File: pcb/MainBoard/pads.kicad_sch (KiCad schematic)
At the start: 35 parts

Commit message: pcb: main board - contd
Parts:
- added JP? (x2): SolderJumper_2_Open, Jumper:SolderJumper-2_P1.3mm_Open_RoundedPad1.0x1.5mm, symbol Jumper:SolderJumper_2_Open
- added JP?: SolderJumper_3_Open, Jumper:SolderJumper-3_P1.3mm_Open_RoundedPad1.0x1.5mm, symbol Jumper:SolderJumper_3_Open
- added Q?: HL2304, PCM_Package_TO_SOT_SMD_AKL:SOT-23, symbol Device:Q_NMOS_GSD
- added R? (x6): 10k, Resistor_SMD:R_0402_1005Metric, symbol Device:R
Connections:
- net +3V3: now also JP?.2 (B), Q?.1 (G), R?.1, R?.1; no longer D?.1 (A1), J?.1 (Pin_1)
- net +5V: now also JP?.2 (B), R?.1
- net COL_RCLK: no longer J?.1 (Pin_1)
- net COL_SER: now also JP?.1 (A), Q?.2 (S), R?.2; no longer J?.1 (Pin_1)
- net COL_SRCLK: no longer J?.1 (Pin_1)
- net COL_~{OE}: now also R?.2; no longer J?.1 (Pin_1)
- net COL_~{SRCLR}: now also R?.1; no longer J?.1 (Pin_1)
- net GND: now also R?.2, R?.2
- net ROW_~{OE}: now also R?.2
- net ROW_~{SRCLR}: now also R?.1
- new net COL_RCLK_OUT: J?.1 (Pin_1)
- new net COL_SER_5V: JP?.3 (B), Q?.3 (D), R?.2
- new net COL_SER_OUT: J?.1 (Pin_1), JP?.2 (C)
- new net COL_SRCLK_OUT: J?.1 (Pin_1)
- new net COL_VCC: D?.1 (A1), J?.1 (Pin_1), JP?.1 (A), JP?.1 (A), R?.1
- new net COL_~{OE}_OUT: J?.1 (Pin_1)
- new net COL_~{SRCLR}_OUT: J?.1 (Pin_1)
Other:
- note added: "clear and disable output by default"
- note added: "rows don't need vled"
- moved on the sheet: D?, J?, R?

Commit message: pcb progress
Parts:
- D501, D502, D503, D504, D505, D506, D507, D508, D509, D510, D511, D512, D513, D514: renamed from D?; footprint can:DFN1006_TVS -> led-matrix:DFN1006_TVS
- gave numbers to parts that had none: 31

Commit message: dump pcb
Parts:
- removed JP501, JP502: SolderJumper_2_Open, Jumper:SolderJumper-2_P1.3mm_Open_RoundedPad1.0x1.5mm, symbol Jumper:SolderJumper_2_Open
- added C501, C504, C505: 22u, Capacitor_SMD:C_0805_2012Metric, symbol Device:C
- added C502: 470u, Capacitor_SMD:CP_Elec_8x10.5, symbol Device:C_Polarized
- added C503: 100u, Capacitor_Tantalum_SMD:CP_EIA-3528-15_AVX-H, symbol Device:C_Polarized
- added H501, H502, H503, H504: JLCToolingHole, led-matrix:jlcpcb-tooling-hole, symbol Mechanical:MountingHole
- added JP501, JP502, JP504, JP505, JP506, JP507, JP508, JP509: SolderJumper_3_Open, led-matrix:SolderJumper-3_Open_RoundedPad_Smol, symbol Jumper:SolderJumper_3_Open
- added Q502, Q503, Q504, Q505, Q506, Q507: HL2304, Package_TO_SOT_SMD:SOT-23, symbol Device:Q_NMOS_GSD
- added R508, R510, R512, R513, R515: 4k7, Resistor_SMD:R_0402_1005Metric, symbol Device:R
- added R509, R511, R514: 10k, Resistor_SMD:R_0402_1005Metric, symbol Device:R
- JP503: footprint Jumper:SolderJumper-3_P1.3mm_Open_RoundedPad1.0x1.5mm -> led-matrix:SolderJumper-3_Open_RoundedPad_Smol
- Q501: footprint PCM_Package_TO_SOT_SMD_AKL:SOT-23 -> Package_TO_SOT_SMD:SOT-23
- R501, R507: value 10k -> 4k7; LCSC C25744 -> C25900
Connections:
- net +3V3: now also C501.1, C505.1, JP501.1 (A), Q507.1 (G), R514.1
- net +5V: now also R501.1, C502.1, C503.1, JP501.3 (B), JP504.1 (A), R508.1, R510.1, R512.1, R513.1, R515.1
- net COL_RCLK: now also JP502.1 (A), Q502.1 (G), R509.1; no longer D507.1 (A1)
- net COL_RCLK_OUT: now also D507.1 (A1), JP502.2 (C)
- net COL_SER: now also JP507.1 (A), Q505.1 (G); no longer D505.1 (A1), JP503.1 (A)
- net COL_SER_5V: now also Q505.3 (D); no longer Q501.3 (D)
- net COL_SER_OUT: now also D505.1 (A1), JP507.2 (C); no longer JP503.2 (C)
- net COL_SRCLK: now also JP506.1 (A), Q504.1 (G), R511.1; no longer D508.1 (A1)
- net COL_SRCLK_OUT: now also D508.1 (A1), JP506.2 (C)
- net COL_VCC: now also C504.1, JP501.2 (C); no longer R501.1
- net COL_~{OE}: now also R504.1, JP505.1 (A), Q503.1 (G); no longer D506.1 (A1), R501.2
- net COL_~{OE}_OUT: now also D506.1 (A1), JP505.2 (C)
- net COL_~{SRCLR}: now also JP509.1 (A), Q506.1 (G), Q507.2 (S), R514.2; no longer D509.1 (A1), R504.1
- net COL_~{SRCLR}_OUT: now also D509.1 (A1), JP509.2 (C)
- net GND: now also C501.2, C502.2, C503.2, C504.2, C505.2, Q502.2 (S), Q503.2 (S), Q504.2 (S), Q505.2 (S), Q506.2 (S), R509.2, R511.2
- net ROW_VLED: now also JP504.2 (C); no longer R503.1
- new net: JP503.2 (C), JP507.3 (B)
- new net: JP504.3 (B), R503.1
- new net: JP508.2 (C), JP509.3 (B)
- new net COL_RCLK_5V: JP502.3 (B), Q502.3 (D), R508.2
- new net COL_SER_5V_BIDI: JP503.1 (A), Q501.3 (D), R512.2
- new net COL_SRCLK_5V: JP506.3 (B), Q504.3 (D), R510.2
- new net COL_~{OE}_5V: JP505.3 (B), Q503.3 (D), R501.2
- new net COL_~{SRCLR}_5V: JP508.3 (B), Q506.3 (D), R513.2
- new net COL_~{SRCLR}_5V_BIDI: JP508.1 (A), Q507.3 (D), R515.2
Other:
- note added: "rows don't need vled… I think"
- note removed: "rows don't need vled"
- moved on the sheet: J501, J502, J503, J504, J505, J506, J507, J508, J509, J510, J511, J512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

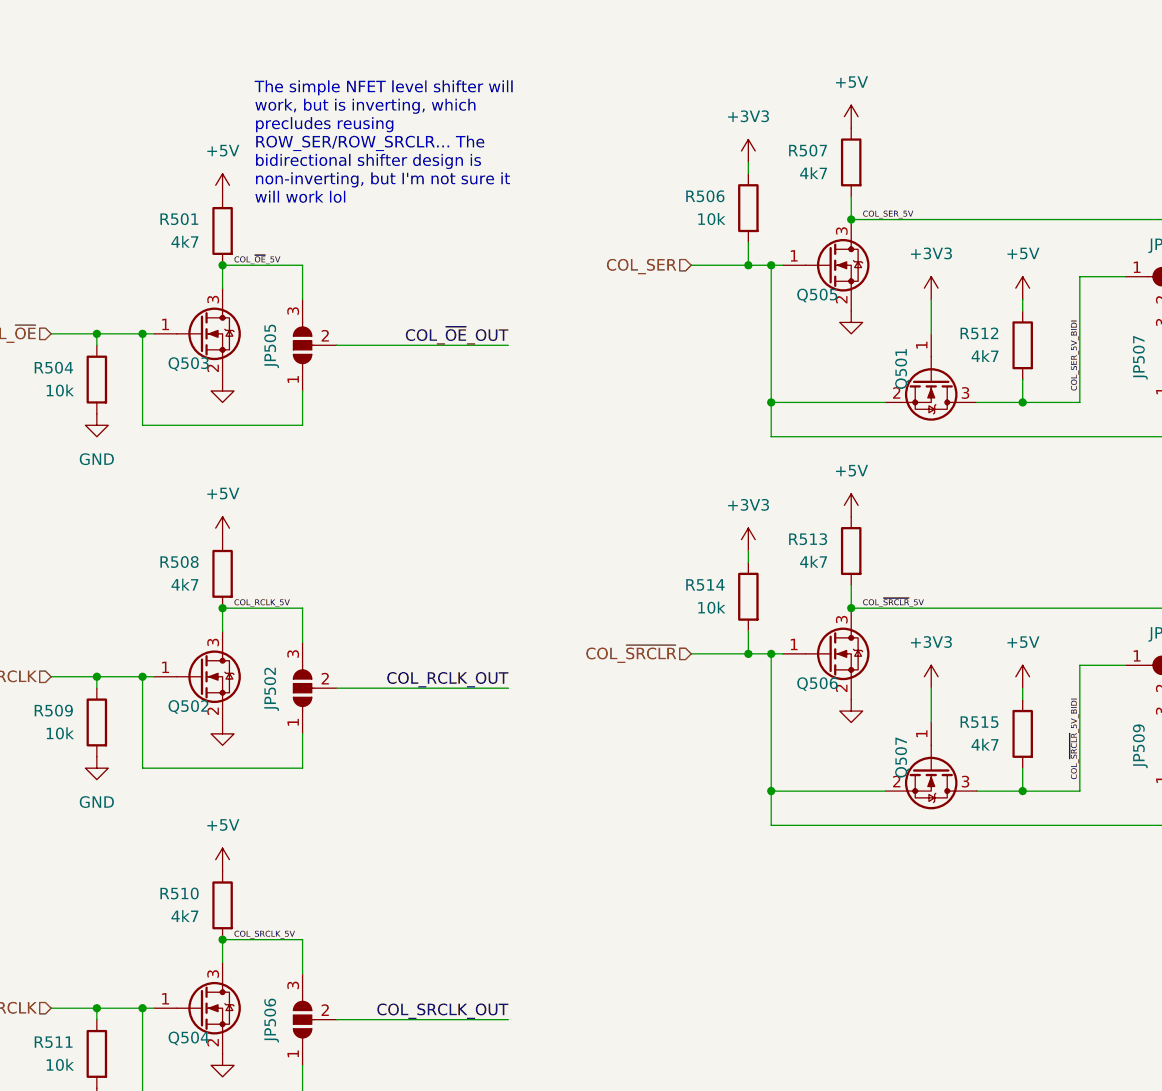
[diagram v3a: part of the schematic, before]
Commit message: MainBoard: fixes, simplify, BOM optimize, DRC fixes, ERC fixes
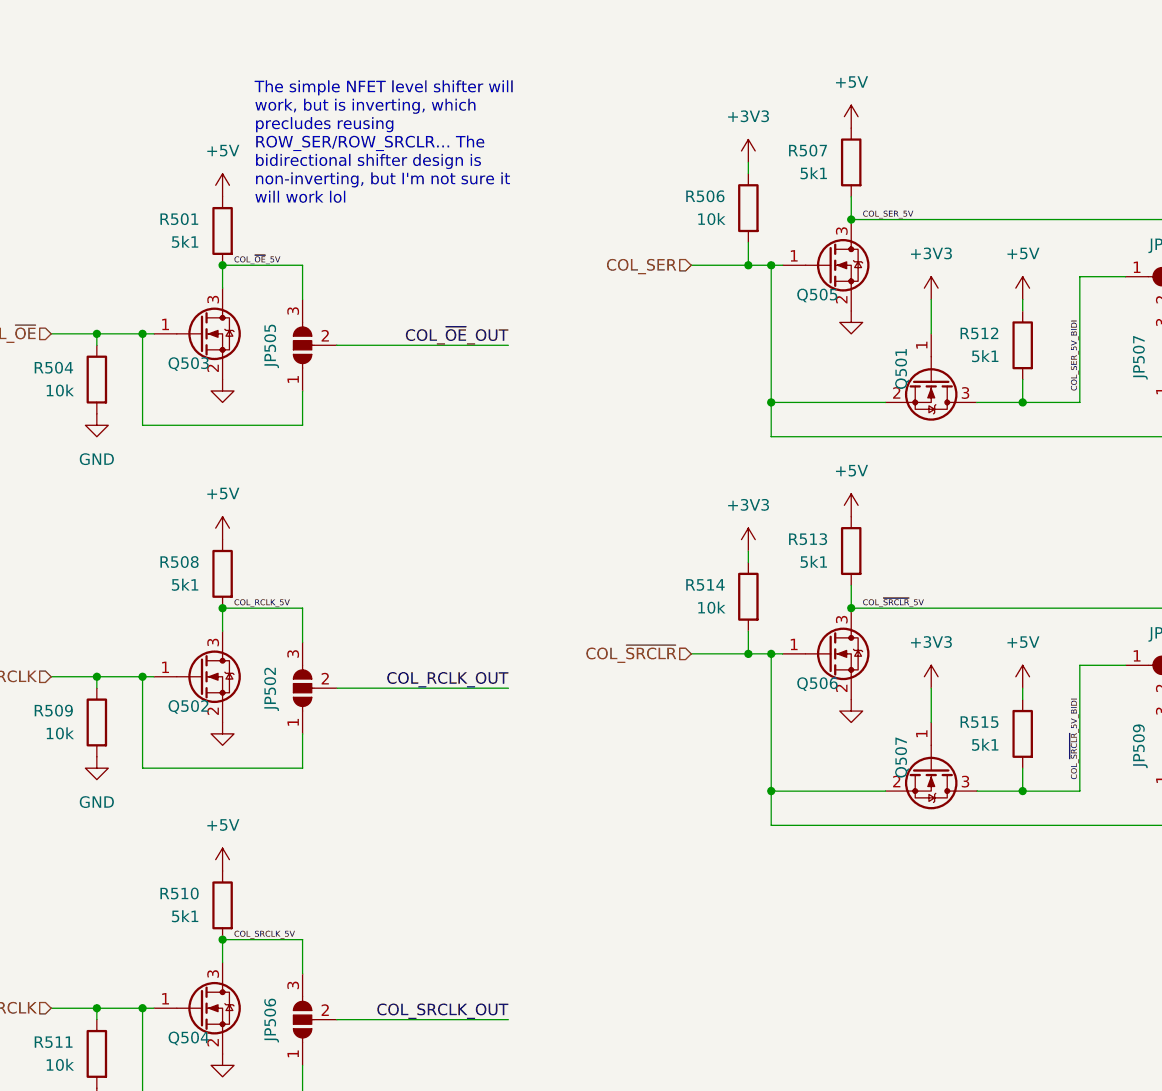
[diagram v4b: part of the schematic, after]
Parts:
- J501, J502, J503, J504, J505, J506, J507, J508, J509, J510, J511, J512, J513, J514, J515, J516, J517, J518, J519, J520, JP501, JP502, JP503, JP504, JP505, JP506, JP507, JP508, JP509: now left out of the parts list
- R501, R507, R508, R510, R512, R513, R515: value 4k7 -> 5k1; LCSC C25900 -> C25905
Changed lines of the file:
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@@
 		(unit 1)
 		(exclude_from_sim no)
-		(in_bom yes)
+		(in_bom no)
 		(on_board yes)
 		(dnp no)
@@
 			)
 		)
-		(property "Value" "4k7"
+		(property "Value" "5k1"
 			(at 91.44 96.5199 0)
 			(effects
@@
 			)
 		)
-		(property "LCSC" "C25900"
+		(property "LCSC" "C25905"
 			(at 93.98 95.25 0)
 			(effects
@@
 		(unit 1)
 		(exclude_from_sim no)
-		(in_bom yes)
+		(in_bom no)
 		(on_board yes)
 		(dnp no)
@@
 		(unit 1)
 		(exclude_from_sim no)
-		(in_bom yes)
+		(in_bom no)
 		(on_board yes)
 		(dnp no)
@@
 		(unit 1)
 		(exclude_from_sim no)
-		(in_bom yes)
+		(in_bom no)
 		(on_board yes)
 		(dnp no)
@@
 		(unit 1)
 		(exclude_from_sim no)
-		(in_bom yes)
+		(in_bom no)
 		(on_board yes)
 		(dnp no)
@@
 			)
 		)
-		(property "Value" "4k7"
+		(property "Value" "5k1"
 			(at 161.29 88.8999 0)
 			(effects
@@
 			)
 		)
-		(property "LCSC" "C25900"
+		(property "LCSC" "C25905"
 			(at 163.83 87.63 0)
 			(effects
@@
 		(unit 1)
 		(exclude_from_sim no)
-		(in_bom yes)
+		(in_bom no)
 		(on_board yes)
 		(dnp no)
@@
 		(unit 1)
 		(exclude_from_sim no)
-		(in_bom yes)
+		(in_bom no)
 		(on_board yes)
 		(dnp no)
@@
 		(unit 1)
 		(exclude_from_sim no)
-		(in_bom yes)
+		(in_bom no)
 		(on_board yes)
 		(dnp no)
@@
 		(unit 1)
 		(exclude_from_sim no)
-		(in_bom yes)
+		(in_bom no)
 		(on_board yes)
 		(dnp no)
@@
 		(unit 1)
 		(exclude_from_sim no)
-		(in_bom yes)
+		(in_bom no)
 		(on_board yes)
 		(dnp no)
@@
 			)
 		)
-		(property "Value" "4k7"
+		(property "Value" "5k1"
 			(at 161.29 132.0799 0)
 			(effects
@@
 			)
 		)
-		(property "LCSC" "C25900"
+		(property "LCSC" "C25905"
 			(at 163.83 130.81 0)
 			(effects
@@
 		(unit 1)
 		(exclude_from_sim no)
-		(in_bom yes)
+		(in_bom no)
 		(on_board yes)
 		(dnp no)
@@
 		(unit 1)
 		(exclude_from_sim no)
-		(in_bom yes)
+		(in_bom no)
 		(on_board yes)
 		(dnp no)
@@
 		(unit 1)
 		(exclude_from_sim no)
-		(in_bom yes)
+		(in_bom no)
 		(on_board yes)
 		(dnp no)
@@
 		(unit 1)
 		(exclude_from_sim no)
-		(in_bom yes)
+		(in_bom no)
 		(on_board yes)
 		(dnp no)
@@
 		(unit 1)
 		(exclude_from_sim no)
-		(in_bom yes)
+		(in_bom no)
 		(on_board yes)
 		(dnp no)
@@
 		(unit 1)
 		(exclude_from_sim no)
-		(in_bom yes)
+		(in_bom no)
 		(on_board yes)
 		(dnp no)
@@
 		(unit 1)
 		(exclude_from_sim no)
-		(in_bom yes)
+		(in_bom no)
 		(on_board yes)
 		(dnp no)
@@
 			)
 		)
-		(property "Value" "4k7"
+		(property "Value" "5k1"
 			(at 180.34 109.2199 0)
 			(effects
@@
 			)
 		)
-		(property "LCSC" "C25900"
+		(property "LCSC" "C25905"
 			(at 182.88 107.95 0)
 			(effects
@@
 		(unit 1)
 		(exclude_from_sim no)
-		(in_bom yes)
+		(in_bom no)
 		(on_board yes)
 		(dnp no)
@@
 			)
 		)
-		(property "Value" "4k7"
+		(property "Value" "5k1"
 			(at 180.34 152.3999 0)
 			(effects
@@
 			)
 		)
-		(property "LCSC" "C25900"
+		(property "LCSC" "C25905"
 			(at 182.88 151.13 0)
 			(effects
@@
 		(unit 1)
 		(exclude_from_sim no)
-		(in_bom yes)
+		(in_bom no)
 		(on_board yes)
 		(dnp no)
@@
 			)
 		)
-		(property "Value" "4k7"
+		(property "Value" "5k1"
 			(at 91.44 171.4499 0)
 			(effects
@@
 			)
 		)
-		(property "LCSC" "C25900"
+		(property "LCSC" "C25905"
 			(at 93.98 170.18 0)
 			(effects
@@
 		(unit 1)
 		(exclude_from_sim no)
-		(in_bom yes)
+		(in_bom no)
 		(on_board yes)
 		(dnp no)
@@
 		(unit 1)
 		(exclude_from_sim no)
-		(in_bom yes)
+		(in_bom no)
 		(on_board yes)
 		(dnp no)
@@
 			)
 		)
-		(property "Value" "4k7"
+		(property "Value" "5k1"
 			(at 91.44 134.6199 0)
 			(effects
@@
 			)
 		)
-		(property "LCSC" "C25900"
+		(property "LCSC" "C25905"
 			(at 93.98 133.35 0)
 			(effects
@@
 		(unit 1)
 		(exclude_from_sim no)
-		(in_bom yes)
+		(in_bom no)
 		(on_board yes)
 		(dnp no)
@@
 		(unit 1)
 		(exclude_from_sim no)
-		(in_bom yes)
+		(in_bom no)
 		(on_board yes)
 		(dnp no)
@@
 		(unit 1)
 		(exclude_from_sim no)
-		(in_bom yes)
+		(in_bom no)
 		(on_board yes)
 		(dnp no)
@@
 		(unit 1)
 		(exclude_from_sim no)
-		(in_bom yes)
+		(in_bom no)
 		(on_board yes)
 		(dnp no)
@@
 		(unit 1)
 		(exclude_from_sim no)
-		(in_bom yes)
+		(in_bom no)
 		(on_board yes)
 		(dnp no)
@@
 		(unit 1)
 		(exclude_from_sim no)
-		(in_bom yes)
+		(in_bom no)
 		(on_board yes)
 		(dnp no)
@@
 		(unit 1)
 		(exclude_from_sim no)
-		(in_bom yes)
+		(in_bom no)
 		(on_board yes)
 		(dnp no)
@@
 		(unit 1)
 		(exclude_from_sim no)
-		(in_bom yes)
+		(in_bom no)
 		(on_board yes)
 		(dnp no)

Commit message: pcb: fixes, improvements
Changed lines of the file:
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@@
+		)
+	)
+	(text_box "470u could be too much"
+		(exclude_from_sim no)
+		(at 15.24 13.97 0)
+		(size 34.29 3.81)
+		(stroke
+			(width -0.0001)
+			(type default)
+		)
+		(fill
+			(type none)
+		)
+		(effects
+			(font
+				(size 1.27 1.27)
+			)
+			(justify left top)
 		)
 	)
